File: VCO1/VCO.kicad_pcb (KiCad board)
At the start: 2 copper layers, 77 parts, among them J5 PANEL, J9 POWER, Q1 THAT340, Q2 2N3904, Q3 2N3904, U1 TL074, U2 TL072, U3 CA3080

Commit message: update pcb
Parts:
- added J10: Panel Power, Connector_PinHeader_2.54mm:PinHeader_1x03_P2.54mm_Vertical, F.Cu at (88.9, 118.1)
- RV5: value 100 - V/OCT -> 100 - V/OCT Trim
- RV6: value 100k (TRIM) -> 100k - High Freq Trim
- RV7: value 100k (TRIM) -> 100k - Sine Round Trim
- RV8: value 50k (TRIM) -> 50k - Sine Symetrie Trim
- moved R34 56.4 mm to (105.3, 115.4)
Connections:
- J5 pad 2: /Sine -> /INITIAL
- J5 pad 3: /Triangle -> /PWM
- J5 pad 4: /INITIAL -> /Sine
- J5 pad 5: /PWM -> /LIN_FM
- J5 pad 6: /LIN_FM -> /EXP_FM
- J5 pad 7: /EXP_FM -> /FINE
- J5 pad 8: /FINE -> /Triangle
- J9 pad 1: -15V -> +5V
- J9 pad 10: +5V -> -15V
- J9 pad 2: -15V -> +5V
- J9 pad 3: +15V -> GND
- J9 pad 4: +15V -> GND
- J9 pad 7: GND -> +15V
- J9 pad 8: GND -> +15V
- J9 pad 9: +5V -> -15V
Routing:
- net GND: track 37.7 -> 385.1 mm
- net Net-(C11-Pad1): track 119.1 -> 53.4 mm
- net /Triangle: track 9.41 -> 50.7 mm
- net -15V: track 153.7 -> 178.0 mm
- net Net-(C10-Pad2): track 76.4 -> 61.0 mm
- net +5V: track 166.4 -> 154.1 mm
- net Net-(Q1-Pad9): track 53.9 -> 61.2 mm
- net Net-(Q1-Pad12): track 42.8 -> 49.7 mm, vias 1 -> 0
- net Net-(Q1-Pad3): track 45.0 -> 40.1 mm
- net /INITIAL: track 8.14 -> 4.34 mm
- net Net-(R11-Pad1): track 26.5 -> 23.0 mm
- net /PWM: track 7.26 -> 3.81 mm
- net Net-(Q1-Pad1): track 48.0 -> 50.2 mm
- net Net-(R1-Pad1): track 47.0 -> 45.0 mm
- net /LIN_FM: track 19.1 -> 17.3 mm
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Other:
- board text added: "High Freq"
- board text added: "Sine Round"
- board text added: "Sine Symetry"
- board text added: "V/OCT"

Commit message: update vco1 pcb
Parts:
- added G***: LOGO, logo:spielhuus, F.Cu at (149.6, 78.6)
- added REF**: MountingHole_2.2mm_M2_ISO7380, MountingHole:MountingHole_2.2mm_M2_ISO7380, F.Cu at (164.5, 133.6)
- added REF**: MountingHole_2.2mm_M2_ISO7380, MountingHole:MountingHole_2.2mm_M2_ISO7380, F.Cu at (62.2, 133.6)
- added REF**: MountingHole_2.2mm_M2_ISO7380, MountingHole:MountingHole_2.2mm_M2_ISO7380, F.Cu at (62.2, 73.7)
- added REF**: MountingHole_2.2mm_M2_ISO7380, MountingHole:MountingHole_2.2mm_M2_ISO7380, F.Cu at (164.5, 73.7)
- moved R16 26.1 mm to (142.2, 123.2), turned to 90 degrees
- moved R30 17.8 mm to (124.5, 108.0)
- moved R22 17.8 mm to (116.8, 111.8)
- moved C11 14.0 mm to (127.0, 100.3)
- moved R21 13.7 mm to (128.3, 114.3)
- moved R10 13.3 mm to (86.4, 85.1)
- moved R36 12.7 mm to (99.1, 73.7)
- moved R15 10.9 mm to (134.6, 111.8)
- moved R20 8.52 mm to (124.5, 115.6)
- moved R11 7.62 mm to (90.2, 113.0), turned to 180 degrees
- moved R43 7.62 mm to (163.8, 115.6), turned to 90 degrees
- moved C1 6.35 mm to (73.7, 113.0)
- moved C2 6.35 mm to (73.7, 106.7)
- moved C6 5.04 mm to (146.1, 85.1)
- moved R27 3.81 mm to (134.6, 108.0)
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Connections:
- D2 pad 1: +5V -> Net-(D2-Pad1)
- D2 pad 2: Net-(D2-Pad2) -> +5V
- D3 pad 1: +5V -> Net-(D3-Pad1)
- D3 pad 2: Net-(D3-Pad2) -> +5V
- D4 pad 1: +5V -> Net-(D4-Pad1)
- D4 pad 2: Net-(D4-Pad2) -> +5V
- D5 pad 1: +5V -> Net-(D5-Pad1)
- D5 pad 2: Net-(D5-Pad2) -> +5V
- D6 pad 1: +5V -> Net-(D6-Pad1)
- D6 pad 2: Net-(D6-Pad2) -> +5V
- D7 pad 1: +5V -> Net-(D7-Pad1)
- D7 pad 2: Net-(D7-Pad2) -> +5V
- D8 pad 1: +5V -> Net-(D8-Pad1)
- D8 pad 2: Net-(D8-Pad2) -> +5V
- D9 pad 1: +5V -> Net-(D9-Pad1)
- D9 pad 2: Net-(D9-Pad2) -> +5V
- R37 pad 2: Net-(D2-Pad2) -> Net-(D2-Pad1)
- R38 pad 2: Net-(D3-Pad2) -> Net-(D3-Pad1)
- R39 pad 2: Net-(D4-Pad2) -> Net-(D4-Pad1)
- R40 pad 2: Net-(D5-Pad2) -> Net-(D5-Pad1)
- R41 pad 2: Net-(D6-Pad2) -> Net-(D6-Pad1)
- R42 pad 2: Net-(D7-Pad2) -> Net-(D7-Pad1)
- R43 pad 2: Net-(D8-Pad2) -> Net-(D8-Pad1)
- R44 pad 2: Net-(D9-Pad2) -> Net-(D9-Pad1)
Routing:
- net GND: track 385.1 -> 209.8 mm
- net +5V: track 154.1 -> 195.4 mm
- net Net-(Q1-Pad9): track 61.2 -> 87.4 mm
- net /Triangle: track 50.7 -> 76.1 mm
- net -15V: track 178.0 -> 200.9 mm
- net Net-(C12-Pad2): track 31.5 -> 48.8 mm
- net Net-(C11-Pad1): track 53.4 -> 70.1 mm
- net Net-(Q3-Pad3): track 12.2 -> 27.6 mm
- net Net-(D8-Pad2): track 13.2 -> 0.00 mm
- net /Pulse: track 19.0 -> 31.6 mm
- net Net-(Q2-Pad1): track 27.8 -> 15.8 mm
- net Net-(Q1-Pad10): track 20.1 -> 30.1 mm
- net Net-(D6-Pad1): track 0.00 -> 8.10 mm
- net Net-(D5-Pad1): track 0.00 -> 7.54 mm
- net Net-(D2-Pad1): track 0.00 -> 7.54 mm
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- added copper zone on B.Cu, net GND
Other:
- board outline added: 107.3 x 65 mm
- board text added: "Rev01"
- board text added: "VCO-1"

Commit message: check pcb
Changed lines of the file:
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@@
-(kicad_pcb (version 20171130) (host pcbnew 5.1.2)
+(kicad_pcb (version 20171130) (host pcbnew "(5.0.1)-4")
   (general
     (thickness 1.6)
@@
   (layers
     (0 F.Cu signal)
-    (31 B.Cu signal)
+    (31 B.Cu signal hide)
     (32 B.Adhes user)
     (33 F.Adhes user)
@@
   )
   (setup
-    (last_trace_width 0.762)
+    (last_trace_width 0.25)
     (user_trace_width 0.762)
     (user_trace_width 1.016)
@@
     (zone_45_only no)
     (trace_min 0.2)
+    (segment_width 0.2)
+    (edge_width 0.05)
     (via_size 0.8)
     (via_drill 0.4)
@@
     (uvia_min_size 0.2)
     (uvia_min_drill 0.1)
-    (edge_width 0.05)
-    (segment_width 0.2)
     (pcb_text_width 0.3)
     (pcb_text_size 1.5 1.5)
@@
     (solder_mask_min_width 0.25)
     (aux_axis_origin 0 0)
-    (visible_elements FFFFFF7F)
+    (visible_elements 7FFFFFFF)
     (pcbplotparams
       (layerselection 0x010fc_ffffffff)
@@
     (descr "Potentiometer, horizontal, Bourns 3296Z, https://www.bourns.com/pdfs/3296.pdf")
     (tags "Potentiometer horizontal Bourns 3296Z")
-    (fp_text reference RV5 (at -3.3 -2.4 90) (layer F.SilkS)
+    (fp_text reference RV5 (at -6.12 -2.57 90) (layer F.SilkS)
       (effects (font (size 1 1) (thickness 0.15)))
     )
@@
     (descr "C, Disc series, Radial, pin pitch=2.50mm, , diameter*width=3.4*2.1mm^2, Capacitor, http://www.vishay.com/docs/45233/krseries.pdf")
     (tags "C Disc series Radial pin pitch 2.50mm  diameter 3.4mm width 2.1mm Capacitor")
-    (fp_text reference C11 (at 1.25 -2.3) (layer F.SilkS)
+    (fp_text reference C11 (at 1.32 2.21) (layer F.SilkS)
       (effects (font (size 1 1) (thickness 0.15)))
     )
@@
     (descr "C, Disc series, Radial, pin pitch=2.50mm, , diameter*width=3.4*2.1mm^2, Capacitor, http://www.vishay.com/docs/45233/krseries.pdf")
     (tags "C Disc series Radial pin pitch 2.50mm  diameter 3.4mm width 2.1mm Capacitor")
-    (fp_text reference C9 (at 1.25 -2.3) (layer F.SilkS)
+    (fp_text reference C9 (at 1.02 2.21) (layer F.SilkS)
       (effects (font (size 1 1) (thickness 0.15)))
     )
@@
     (descr "C, Disc series, Radial, pin pitch=2.50mm, , diameter*width=3.4*2.1mm^2, Capacitor, http://www.vishay.com/docs/45233/krseries.pdf")
     (tags "C Disc series Radial pin pitch 2.50mm  diameter 3.4mm width 2.1mm Capacitor")
-    (fp_text reference C7 (at 1.25 -2.3) (layer F.SilkS)
+    (fp_text reference C7 (at 1.12 1.7) (layer F.SilkS)
       (effects (font (size 1 1) (thickness 0.15)))
     )
@@
     (descr "TO-92 leads in-line, narrow, oval pads, drill 0.75mm (see NXP sot054_po.pdf)")
     (tags "to-92 sc-43 sc-43a sot54 PA33 transistor")
-    (fp_text reference Q3 (at 1.27 2.54 90) (layer F.SilkS)
+    (fp_text reference Q3 (at 1.27 -3.175 90) (layer F.SilkS)
       (effects (font (size 1 1) (thickness 0.15)))
     )
@@
     (descr "C, Radial series, Radial, pin pitch=2.00mm, diameter=5mm, height=11mm, Non-Polar Electrolytic Capacitor")
     (tags "C Radial series Radial pin pitch 2.00mm diameter 5mm height 11mm Non-Polar Electrolytic Capacitor")
-    (fp_text reference C1 (at 1 -3.75) (layer F.SilkS)
+    (fp_text reference C1 (at 0.96 3.43) (layer F.SilkS)
       (effects (font (size 1 1) (thickness 0.15)))
     )
@@
     (effects (font (size 1 1) (thickness 0.15)))
   )
-  (gr_text VCO-1 (at 151.91 73.5 180) (layer F.SilkS)
+  (gr_text VCO-1 (at 151.89 74.12 180) (layer F.SilkS)
     (effects (font (size 1 1) (thickness 0.15)))
   )

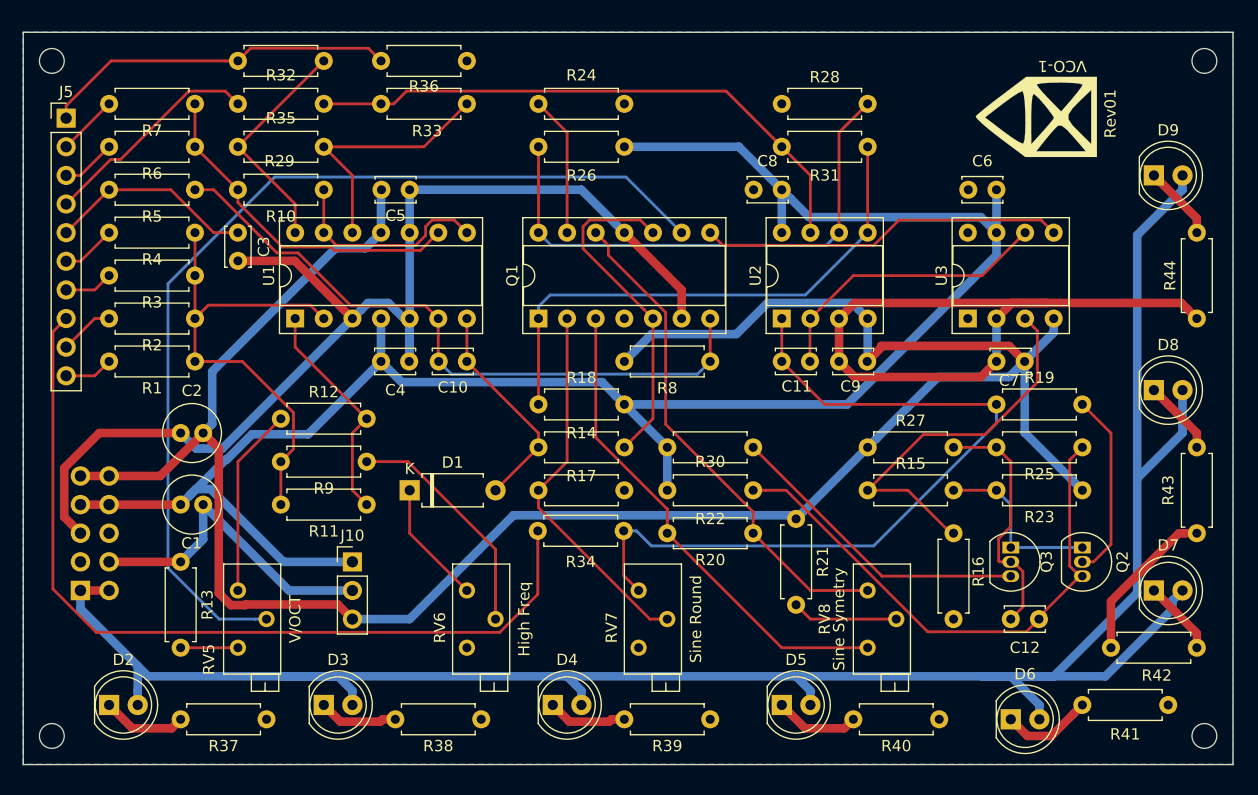
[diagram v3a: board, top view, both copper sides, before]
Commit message: finalizy modules: ADSR, Bass++ and VCO1
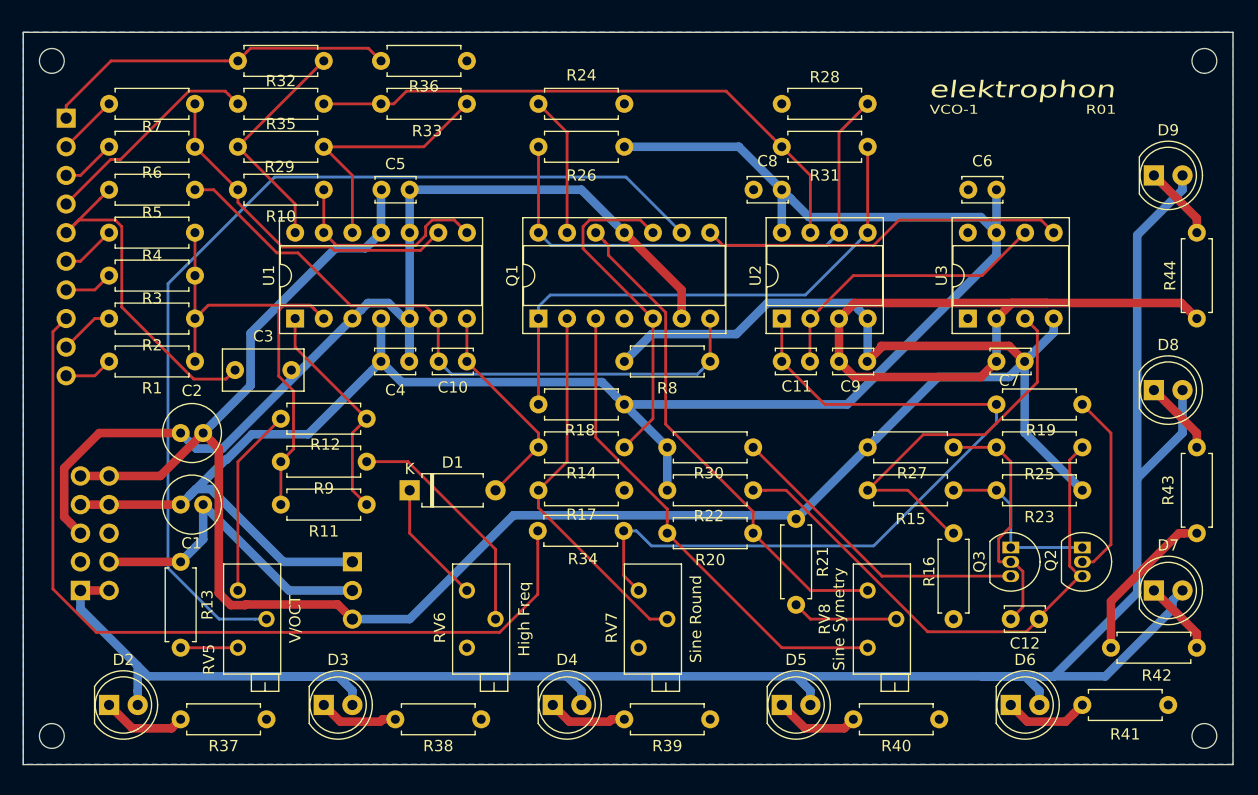
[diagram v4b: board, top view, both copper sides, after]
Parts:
- removed G***: LOGO, logo:spielhuus
- C3: footprint Capacitor_THT:C_Disc_D3.4mm_W2.1mm_P2.50mm -> Capacitor_THT:C_Rect_L7.0mm_W3.5mm_P5.00mm
- J10, J5: moved to B.Cu
- moved C3 12.2 mm to (78.5, 101.1), turned to 0 degrees
- moved D6 1.27 mm to (147.3, 130.8)
- turned J10 to 180 degrees
- turned J5 to 180 degrees
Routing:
- net /LIN_FM: track 18.4 -> 31.2 mm
- net GND: track 209.8 -> 197.5 mm
- net Net-(R1-Pad1): track 43.1 -> 45.6 mm
- net +5V: track 195.4 -> 193.6 mm
- net Net-(D6-Pad1): track 8.10 -> 7.58 mm
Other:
- board text added: "+15V"
- board text added: "-15V"
- board text added: "1"
- board text added: "10"
- board text added: "2"
- board text added: "3"
- board text added: "4"
- board text added: "5"
- board text added: "5V"
- board text added: "6"
- board text added: "7"
- board text added: "8"
- board text added: "9"
- board text added: "GND"
- board text added: "R01"
- board text added: "elektrophon"
- board text removed: "Rev01"
